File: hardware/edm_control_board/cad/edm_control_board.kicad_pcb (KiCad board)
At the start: 2 copper layers, 240 x 100 mm, 60 parts, among them J501 Conn_02x08_Odd_Even, J502 Conn_01x02, Q201 BSS214NW, Q202 BSS214NW, Q203 BSS214NW, Q204 BSS214NW, SW401 SW_Push, SW402 SW_Push, SW403 SW_Push, SW404 SW_Push, U301 STM32F722RETx, U302 R-78E3.3-1.0, U303 L78L05_SO8, U401 NHD-0420H1Z, Y201 25M

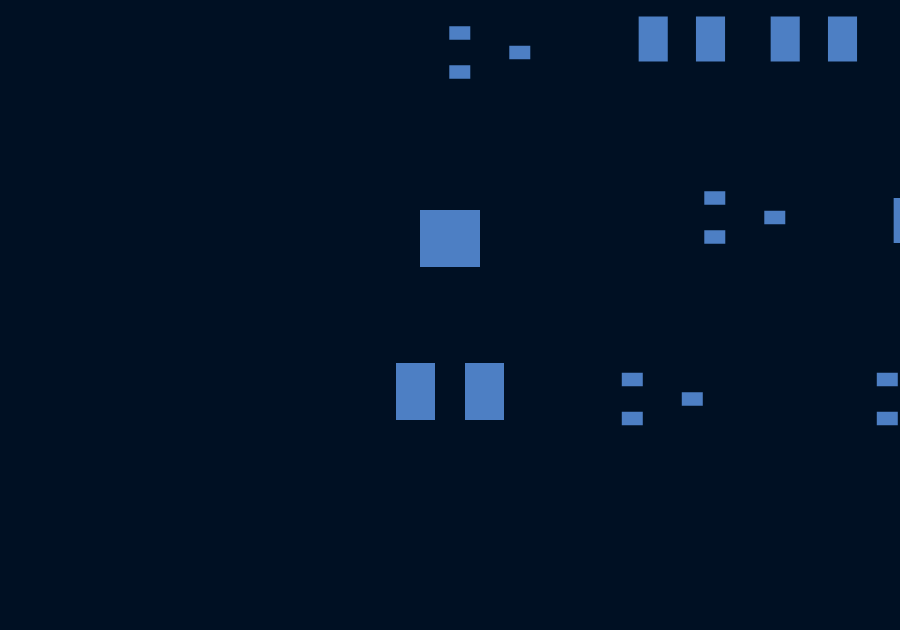
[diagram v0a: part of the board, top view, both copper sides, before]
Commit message: Change to horizontal trim pot
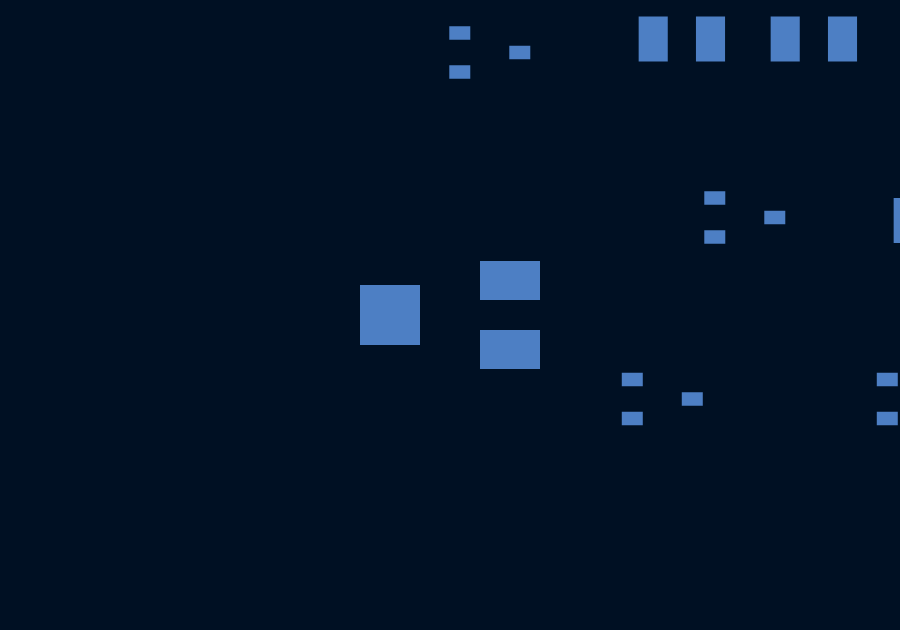
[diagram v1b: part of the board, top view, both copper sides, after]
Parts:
- RV201: footprint Potentiometer_SMD:Potentiometer_Bourns_3214X_Vertical -> Potentiometer_SMD:Potentiometer_Bourns_3214J_Horizontal
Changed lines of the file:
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@@
     (add_net "Net-(U303-Pad5)")
+  )
+  (module Potentiometer_SMD:Potentiometer_Bourns_3214J_Horizontal (layer B.Cu)
+    (at 108.43505 -117.520679)
+    (descr "Potentiometer, horizontal, Bourns 3214J, https://www.bourns.com/docs/Product-Datasheets/3214.pdf")
+    (tags "Potentiometer horizontal Bourns 3214J")
+    (attr smd)
+    (fp_text reference RV201 (at 0 3.65) (layer B.SilkS)
+      (effects (font (size 1 1) (thickness 0.15)) (justify mirror))
+    )
+    (fp_text value 20k (at 0 -3.65) (layer B.Fab)
+      (effects (font (size 1 1) (thickness 0.15)) (justify mirror))
+    )
+    (fp_line (start -2.3 2.4) (end -2.3 -2.4) (layer B.Fab) (width 0.1))
+    (fp_line (start -2.3 -2.4) (end 2.3 -2.4) (layer B.Fab) (width 0.1))
+    (fp_line (start 2.3 -2.4) (end 2.3 2.4) (layer B.Fab) (width 0.1))
+    (fp_line (start 2.3 2.4) (end -2.3 2.4) (layer B.Fab) (width 0.1))
+    (fp_line (start -2.3 2.02) (end -2.3 0.24) (layer B.Fab) (width 0.1))
+    (fp_line (start -2.3 0.24) (end -2.3 0.24) (layer B.Fab) (width 0.1))
+    (fp_line (start -2.3 0.24) (end -2.3 2.02) (layer B.Fab) (width 0.1))
+    (fp_line (start -2.3 2.02) (end -2.3 2.02) (layer B.Fab) (width 0.1))
+    (fp_line (start -2.3 1.13) (end -2.3 1.13) (layer B.Fab) (width 0.1))
+    (fp_line (start -2.42 2.52) (end 2.42 2.52) (layer B.SilkS) (width 0.12))
+    (fp_line (start -2.42 -2.52) (end 2.42 -2.52) (layer B.SilkS) (width 0.12))
+    (fp_line (start -2.42 2.52) (end -2.42 1.24) (layer B.SilkS) (width 0.12))
+    (fp_line (start -2.42 -1.24) (end -2.42 -2.52) (layer B.SilkS) (width 0.12))
+    (fp_line (start 2.42 2.52) (end 2.42 2.04) (layer B.SilkS) (width 0.12))
+    (fp_line (start 2.42 0.26) (end 2.42 -0.26) (layer B.SilkS) (width 0.12))
+    (fp_line (start 2.42 -2.04) (end 2.42 -2.52) (layer B.SilkS) (width 0.12))
+    (fp_line (start -2.42 2.14) (end -2.42 2.14) (layer B.SilkS) (width 0.12))
+    (fp_line (start -2.42 2.14) (end -2.42 1.24) (layer B.SilkS) (width 0.12))
+    (fp_line (start -2.42 2.14) (end -2.42 1.24) (layer B.SilkS) (width 0.12))
+    (fp_line (start -3.25 2.65) (end -3.25 -2.65) (layer B.CrtYd) (width 0.05))
+    (fp_line (start -3.25 -2.65) (end 3.25 -2.65) (layer B.CrtYd) (width 0.05))
+    (fp_line (start 3.25 -2.65) (end 3.25 2.65) (layer B.CrtYd) (width 0.05))
+    (fp_line (start 3.25 2.65) (end -3.25 2.65) (layer B.CrtYd) (width 0.05))
+    (fp_text user %R (at 0 0) (layer B.Fab)
+      (effects (font (size 1 1) (thickness 0.15)) (justify mirror))
+    )
+    (pad 1 smd rect (at 2 1.15) (size 2 1.3) (layers B.Cu B.Paste B.Mask)
+      (net 16 +3V3))
+    (pad 2 smd rect (at -2 0) (size 2 2) (layers B.Cu B.Paste B.Mask)
+      (net 60 /Controller/LCD_V0))
+    (pad 3 smd rect (at 2 -1.15) (size 2 1.3) (layers B.Cu B.Paste B.Mask)
+      (net 14 GND))
+    (model ${KISYS3DMOD}/Potentiometer_SMD.3dshapes/Potentiometer_Bourns_3214J_Horizontal.wrl
+      (at (xyz 0 0 0))
+      (scale (xyz 1 1 1))
+      (rotate (xyz 0 0 0))
+    )
   )
   (module Capacitor_SMD:C_0805_2012Metric (layer B.Cu)
@@
       (at (xyz 0 0 0))
       (scale (xyz 1 1 1))
-      (rotate (xyz 0 0 0))
-    )
-  )
-  (module Potentiometer_SMD:Potentiometer_Bourns_3214X_Vertical (layer B.Cu)
-    (at 108.43505 -117.520679)
-    (descr "Potentiometer, vertical, Bourns 3214X, https://www.bourns.com/docs/Product-Datasheets/3214.pdf")
-    (tags "Potentiometer vertical Bourns 3214X")
-    (attr smd)
-    (fp_text reference RV201 (at -0.1 4.75) (layer B.SilkS)
-      (effects (font (size 1 1) (thickness 0.15)) (justify mirror))
-    )
-    (fp_text value 20k (at -0.1 -4.75) (layer B.Fab)
-      (effects (font (size 1 1) (thickness 0.15)) (justify mirror))
-    )
-    (fp_circle (center -1.3 -0.65) (end -0.55 -0.65) (layer B.Fab) (width 0.1))
-    (fp_line (start -2.5 1.75) (end -2.5 -1.75) (layer B.Fab) (width 0.1))
-    (fp_line (start -2.5 -1.75) (end 2.3 -1.75) (layer B.Fab) (width 0.1))
-    (fp_line (start 2.3 -1.75) (end 2.3 1.75) (layer B.Fab) (width 0.1))
-    (fp_line (start 2.3 1.75) (end -2.5 1.75) (layer B.Fab) (width 0.1))
-    (fp_line (start -1.3 -1.393) (end -1.299 0.092) (layer B.Fab) (width 0.1))
-    (fp_line (start -1.3 -1.393) (end -1.299 0.092) (layer B.Fab) (width 0.1))
-    (fp_line (start 2.04 1.87) (end 2.42 1.87) (layer B.SilkS) (width 0.12))
-    (fp_line (start -2.62 1.87) (end -2.039 1.87) (layer B.SilkS) (width 0.12))
-    (fp_line (start -0.26 1.87) (end 0.26 1.87) (layer B.SilkS) (width 0.12))
-    (fp_line (start -2.62 -1.87) (end -1.24 -1.87) (layer B.SilkS) (width 0.12))
-    (fp_line (start 1.24 -1.87) (end 2.42 -1.87) (layer B.SilkS) (width 0.12))
-    (fp_line (start -2.62 1.87) (end -2.62 -1.87) (layer B.SilkS) (width 0.12))
-    (fp_line (start 2.42 1.87) (end 2.42 -1.87) (layer B.SilkS) (width 0.12))
-    (fp_line (start -2.75 3.75) (end -2.75 -3.75) (layer B.CrtYd) (width 0.05))
-    (fp_line (start -2.75 -3.75) (end 2.55 -3.75) (layer B.CrtYd) (width 0.05))
-    (fp_line (start 2.55 -3.75) (end 2.55 3.75) (layer B.CrtYd) (width 0.05))
-    (fp_line (start 2.55 3.75) (end -2.75 3.75) (layer B.CrtYd) (width 0.05))
-    (fp_text user %R (at 0.5 0) (layer B.Fab)
-      (effects (font (size 0.6 0.6) (thickness 0.15)) (justify mirror))
-    )
-    (pad 1 smd rect (at 1.15 2.55) (size 1.3 1.9) (layers B.Cu B.Paste B.Mask)
-      (net 16 +3V3))
-    (pad 2 smd rect (at 0 -2.55) (size 2 1.9) (layers B.Cu B.Paste B.Mask)
-      (net 60 /Controller/LCD_V0))
-    (pad 3 smd rect (at -1.15 2.55) (size 1.3 1.9) (layers B.Cu B.Paste B.Mask)
-      (net 14 GND))
-    (model ${KISYS3DMOD}/Potentiometer_SMD.3dshapes/Potentiometer_Bourns_3214X_Vertical.wrl
-      (at (xyz 0 0 0))
-      (scale (xyz 1 1 1))

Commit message: Component placement
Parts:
- moved NT301 169.4 mm to (198.0, -8.00)
- moved C208 159.6 mm to (185.5, -60.5)
- moved C209 159.3 mm to (184.5, -52.0)
- moved Y201 159.2 mm to (181.5, -59.4), turned to 270 degrees
- moved R206 158.8 mm to (184.5, -54.5)
- moved C210 150.3 mm to (185.5, -58.0)
- moved R207 149.5 mm to (171.5, -70.0), turned to 90 degrees
- moved C212 146.1 mm to (168.0, -45.5), turned to 180 degrees
- moved C302 142.2 mm to (185.5, -26.5), turned to 90 degrees
- moved C304 137.8 mm to (171.5, -26.5), turned to 90 degrees
- moved C211 137.6 mm to (168.0, -48.0), turned to 180 degrees
- moved U302 131.3 mm to (195.0, -87.0), turned to 90 degrees
- moved C306 127.2 mm to (178.5, -35.0)
- moved U303 123.7 mm to (178.5, -27.5)
- moved C301 118.4 mm to (208.0, -88.0), turned to 90 degrees
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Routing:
- added copper zone on In1.Cu, net +3V3
- added copper zone on In2.Cu, net GND
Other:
- copper layers 2 -> 4

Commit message: Update pinout
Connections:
- U301 pad 14: /Controller/LCD_DB0 -> Net-(U301-Pad14)
- U301 pad 15: /Controller/LCD_DB1 -> Net-(U301-Pad15)
- U301 pad 16: /Controller/LCD_DB2 -> Net-(U301-Pad16)
- U301 pad 17: /Controller/LCD_DB3 -> Net-(U301-Pad17)
- U301 pad 20: /Controller/LCD_DB4 -> /Connectors/Breakdown
- U301 pad 21: /Controller/LCD_DB5 -> /Connectors/Short_Circuit
- U301 pad 22: /Controller/LCD_DB6 -> /Connectors/Output_20V_Enable
- U301 pad 23: /Controller/LCD_DB7 -> /Connectors/Output_250V_Enable
- U301 pad 25: /Connectors/Spark_Voltage_0 -> /Connectors/Spark_Voltage_Status
- U301 pad 26: /Connectors/Spark_Voltage_1 -> /Connectors/Spark_Voltage_2
- U301 pad 27: /Connectors/Spark_Voltage_2 -> /Connectors/Spark_Voltage_1
- U301 pad 28: Net-(U301-Pad28) -> /Connectors/Spark_Voltage_0
- U301 pad 33: Net-(U301-Pad33) -> Net-(Q204-Pad1)
- U301 pad 34: Net-(U301-Pad34) -> Net-(Q203-Pad1)
- U301 pad 35: Net-(U301-Pad35) -> Net-(Q202-Pad1)
- U301 pad 36: Net-(U301-Pad36) -> Net-(Q201-Pad1)
- U301 pad 41: /Controller/LCD_RS -> Net-(U301-Pad41)
- U301 pad 42: /Controller/LCD_RW -> /Controller/LCD_DB1
- U301 pad 43: /Controller/LCD_E -> /Controller/LCD_DB0
- U301 pad 44: Net-(U301-Pad44) -> /Controller/LCD_E
- U301 pad 45: Net-(Q202-Pad1) -> /Controller/LCD_RW
- U301 pad 46: Net-(Q203-Pad1) -> /Controller/LCD_RS
- U301 pad 49: Net-(Q204-Pad1) -> Net-(U301-Pad49)
- U301 pad 50: Net-(Q201-Pad1) -> Net-(U301-Pad50)
- U301 pad 53: Net-(U301-Pad53) -> /Controller/LCD_DB7
- U301 pad 55: /Connectors/Spark_Voltage_Status -> /Controller/LCD_DB6
- U301 pad 56: /Connectors/Output_250V_Enable -> /Controller/LCD_DB5
- U301 pad 57: /Connectors/Output_20V_Enable -> /Controller/LCD_DB4
- U301 pad 58: /Connectors/Short_Circuit -> /Controller/LCD_DB3
- U301 pad 59: /Connectors/Breakdown -> /Controller/LCD_DB2

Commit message: Update pinout
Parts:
- moved C208 1.50 mm to (185.5, -62.0)
- moved C210 1.50 mm to (185.5, -59.5)
- moved Y201 1.50 mm to (181.5, -60.9)
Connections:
- RV401 pad 2: /User Interface/POT_1 -> /Controller/POT_1
- RV402 pad 2: /User Interface/POT_2 -> /Controller/POT_2
- RV403 pad 2: /User Interface/POT_3 -> /Controller/POT_3
- RV404 pad 2: /User Interface/POT_4 -> /Controller/POT_4
- SW401 pad 1: /User Interface/SW_1 -> /Controller/SW_1
- SW402 pad 1: /User Interface/SW_2 -> /Controller/SW_2
- SW403 pad 1: /User Interface/SW_3 -> /Controller/SW_3
- SW404 pad 1: /User Interface/SW_4 -> /Controller/SW_4
- U301 pad 10: Net-(U301-Pad10) -> /Controller/POT_3
- U301 pad 11: Net-(U301-Pad11) -> /Controller/POT_4
- U301 pad 36: Net-(Q201-Pad1) -> Net-(U301-Pad36)
- U301 pad 37: Net-(U301-Pad37) -> /Controller/SW_1
- U301 pad 38: Net-(U301-Pad38) -> /Controller/SW_2
- U301 pad 39: Net-(U301-Pad39) -> /Controller/SW_3
- U301 pad 40: Net-(U301-Pad40) -> /Controller/SW_4
- U301 pad 41: Net-(U301-Pad41) -> /Controller/LCD_DB1
- U301 pad 42: /Controller/LCD_DB1 -> /Controller/LCD_DB0
- U301 pad 43: /Controller/LCD_DB0 -> /Controller/LCD_E
- U301 pad 44: /Controller/LCD_E -> /Controller/LCD_RW
- U301 pad 45: /Controller/LCD_RW -> /Controller/LCD_RS
- U301 pad 46: /Controller/LCD_RS -> Net-(Q201-Pad1)
- U301 pad 49: Net-(U301-Pad49) -> /Controller/LCD_DB7
- U301 pad 50: Net-(U301-Pad50) -> /Controller/LCD_DB6
- U301 pad 51: Net-(U301-Pad51) -> /Controller/LCD_DB5
- U301 pad 52: Net-(U301-Pad52) -> /Controller/LCD_DB4
- U301 pad 53: /Controller/LCD_DB7 -> /Controller/LCD_DB3
- U301 pad 55: /Controller/LCD_DB6 -> /Controller/LCD_DB2
- U301 pad 56: /Controller/LCD_DB5 -> Net-(U301-Pad56)
- U301 pad 57: /Controller/LCD_DB4 -> Net-(U301-Pad57)
- U301 pad 58: /Controller/LCD_DB3 -> Net-(U301-Pad58)
- U301 pad 59: /Controller/LCD_DB2 -> Net-(U301-Pad59)
- U301 pad 8: Net-(U301-Pad8) -> /Controller/POT_1
- U301 pad 9: Net-(U301-Pad9) -> /Controller/POT_2
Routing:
- net /Controller/LCD_RS: track 0.00 -> 105.9 mm
- net /Controller/SW_4: track 0.00 -> 91.4 mm
- net /Controller/POT_4: track 0.00 -> 89.6 mm
- net /Controller/SW_3: track 0.00 -> 87.9 mm
- net /Controller/SW_2: track 0.00 -> 81.3 mm
- net /Controller/LCD_DB7: track 0.00 -> 80.3 mm
- net /Controller/SW_1: track 0.00 -> 79.4 mm
- net /Controller/LCD_DB6: track 0.00 -> 78.1 mm
- net /Controller/LCD_DB2: track 0.00 -> 77.9 mm
- net /Controller/LCD_DB5: track 0.00 -> 77.9 mm
- net /Controller/LCD_DB4: track 0.00 -> 77.9 mm
- net /Controller/LCD_DB3: track 0.00 -> 77.8 mm
- net /Controller/LCD_RW: track 0.00 -> 68.3 mm
- net /Controller/LCD_E: track 0.00 -> 67.8 mm
- net /Controller/LCD_DB0: track 0.00 -> 66.8 mm
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
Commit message: Routing
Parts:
- moved R202 2.18 mm to (159.5, -35.0), turned to 90 degrees
- moved Q202 2.12 mm to (159.5, -31.0), turned to 270 degrees
- moved R203 1.61 mm to (162.5, -35.0), turned to 90 degrees
- moved Q203 1.58 mm to (162.5, -31.0), turned to 270 degrees
- moved Q204 1.58 mm to (165.5, -31.0), turned to 270 degrees
- moved R204 1.58 mm to (165.5, -35.0), turned to 90 degrees
- moved C202 1.20 mm to (179.0, -54.5)
- moved C209 1.12 mm to (183.5, -52.5)
- moved R206 1.12 mm to (183.5, -55.0)
- moved C211 0.81 mm to (167.6, -47.3)
- moved C212 0.81 mm to (167.6, -44.8)
- moved C203 0.50 mm to (175.5, -50.0)
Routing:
- net /Controller/LCD_RW: track 68.3 -> 144.4 mm
- net /Controller/LCD_E: track 67.8 -> 142.4 mm
- net /Controller/LCD_DB0: track 66.8 -> 140.5 mm
- net /Controller/LCD_DB1: track 65.8 -> 138.5 mm
- net GND: track 17.9 -> 86.1 mm, vias 8 -> 25
- net /Controller/POT_3: track 0.00 -> 59.8 mm, vias 0 -> 2
- net /Connectors/Spark_Voltage_0: track 0.00 -> 45.8 mm
- net /Connectors/Spark_Voltage_1: track 0.00 -> 44.0 mm
- net /Connectors/Spark_Voltage_2: track 0.00 -> 42.4 mm
- net /Connectors/Spark_Voltage_Status: track 0.00 -> 40.8 mm
- net /Controller/LCD_RS: track 105.9 -> 146.3 mm
- net /Connectors/Output_250V_Enable: track 0.00 -> 40.2 mm
- net /Controller/POT_1: track 0.00 -> 35.9 mm
- net /Controller/POT_4: track 89.6 -> 58.1 mm, vias 0 -> 2
- net Net-(Q202-Pad1): track 0.00 -> 28.6 mm
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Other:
- net class Pwr added: clearance 0.3, trace_width 0.5, via_dia 0.8, via_drill 0.4

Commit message: Routing
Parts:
- moved NT301 1.60 mm to (199.6, -8.00)
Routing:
- net +24V: track 4.32 -> 151.2 mm
- net /Controller/SW_2: track 81.3 -> 194.7 mm
- net /Controller/SW_4: track 91.4 -> 201.3 mm
- net /Controller/SW_3: track 87.9 -> 153.5 mm
- net /Controller/SW_1: track 79.4 -> 134.3 mm
- net /Connectors/Stepper_EN: track 0.00 -> 35.9 mm
- net +5V: track 4.32 -> 33.3 mm
- net /Connectors/Stepper_DIR: track 0.00 -> 24.1 mm
- net /Connectors/Stepper_PUL: track 0.00 -> 23.3 mm
- net GND: track 86.1 -> 94.5 mm
- net /Controller/POT_4: track 58.1 -> 50.3 mm
- net /Connectors/Breakdown: track 40.5 -> 42.9 mm
- net /Connectors/Spark_Voltage_0: track 45.8 -> 48.0 mm
- net /Connectors/Short_Circuit: track 40.4 -> 41.6 mm
- net /Connectors/Spark_Voltage_1: track 44.0 -> 45.0 mm

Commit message: Add SWD connector
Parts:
- added J405: Conn_01x06, Connector_PinHeader_2.54mm:PinHeader_1x06_P2.54mm_Vertical, B.Cu at (122.1, -91.1)
- added R401: 1M, Resistor_SMD:R_1206_3216Metric, B.Cu at (216.5, -26.3)
- moved C301 13.0 mm to (195.6, -84.2)
- moved C303 13.0 mm to (174.6, -87.2)
- moved C305 13.0 mm to (165.6, -85.2)
- moved U302 13.0 mm to (182.6, -83.2)
- moved J402 1.00 mm to (206.0, -9.00)
- moved NT301 1.00 mm to (199.6, -9.00)
- renumbered J501 to J401, J502 to J402, JJ503 to J403, JJ504 to J404, RV401 to RV501, RV402 to RV502, RV403 to RV503, RV404 to RV504, SW401 to SW501, SW402 to SW502, SW403 to SW503, SW404 to SW504, U401 to U501
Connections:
- J401 pad 1: /Connectors/+3V3 -> +3V3
- J401 pad 11: /Connectors/GND -> GND
- J401 pad 13: /Connectors/GND -> GND
- J401 pad 15: /Connectors/GND -> GND
- J401 pad 3: /Connectors/GND -> GND
- J401 pad 5: /Connectors/GND -> GND
- J401 pad 7: /Connectors/GND -> GND
- J401 pad 9: /Connectors/GND -> GND
- MK501 pad 1: GND -> /Connectors/Shield
- MK502 pad 1: GND -> /Connectors/Shield
- MK503 pad 1: GND -> /Connectors/Shield
- MK504 pad 1: GND -> /Connectors/Shield
- MK505 pad 1: GND -> /Connectors/Shield
- MK506 pad 1: GND -> /Connectors/Shield
- MK507 pad 1: GND -> /Connectors/Shield
- MK508 pad 1: GND -> /Connectors/Shield
- MK509 pad 1: GND -> /Connectors/Shield
- MK510 pad 1: GND -> /Connectors/Shield
- MK511 pad 1: GND -> /Connectors/Shield
- MK512 pad 1: GND -> /Connectors/Shield
- U301 pad 36: Net-(U301-Pad36) -> /Controller/SW_1
- U301 pad 37: /Controller/SW_1 -> /Controller/SW_2
- U301 pad 38: /Controller/SW_2 -> /Controller/SW_3
- U301 pad 39: /Controller/SW_3 -> /Controller/SW_4
- U301 pad 40: /Controller/SW_4 -> /Controller/LCD_DB1
- U301 pad 41: /Controller/LCD_DB1 -> /Controller/LCD_DB0
- U301 pad 42: /Controller/LCD_DB0 -> /Controller/LCD_E
- U301 pad 43: /Controller/LCD_E -> /Controller/LCD_RW
- U301 pad 44: /Controller/LCD_RW -> /Controller/LCD_RS
- U301 pad 45: /Controller/LCD_RS -> Net-(Q201-Pad1)
- U301 pad 46: Net-(Q201-Pad1) -> /Connectors/SWDIO
- U301 pad 49: /Controller/LCD_DB7 -> /Connectors/SWCLK
- U301 pad 50: /Controller/LCD_DB6 -> /Controller/LCD_DB7
- U301 pad 51: /Controller/LCD_DB5 -> /Controller/LCD_DB6
- U301 pad 52: /Controller/LCD_DB4 -> /Controller/LCD_DB5
- U301 pad 53: /Controller/LCD_DB3 -> /Controller/LCD_DB4
- U301 pad 55: /Controller/LCD_DB2 -> /Connectors/SWO
- U301 pad 56: Net-(U301-Pad56) -> /Controller/LCD_DB3
- U301 pad 57: Net-(U301-Pad57) -> /Controller/LCD_DB2
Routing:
- net /Connectors/SWCLK: track 0.00 -> 70.5 mm, vias 0 -> 1
- net /Connectors/SWDIO: track 0.00 -> 61.3 mm, vias 0 -> 1
- net /Connectors/SWO: track 0.00 -> 60.8 mm, vias 0 -> 1
- net /Connectors/Shield: track 0.00 -> 16.4 mm
- net +24V: track 151.2 -> 139.2 mm
- net GND: track 94.5 -> 97.9 mm, vias 25 -> 27
- net /Controller/LCD_DB4: track 77.9 -> 75.2 mm
- net /Controller/LCD_DB5: track 77.9 -> 75.3 mm
- net /Controller/LCD_DB6: track 78.1 -> 75.6 mm
- net /Controller/LCD_DB7: track 80.3 -> 77.8 mm
- net /Controller/LCD_DB2: track 77.9 -> 75.5 mm
- net /Controller/LCD_DB3: track 77.8 -> 75.5 mm
- net /Controller/POT_1: track 35.9 -> 35.0 mm
- net /Controller/SW_3: track 153.5 -> 153.0 mm
- added copper zone on F.Cu, net /Connectors/Shield
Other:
- board text added: "+24V"
- board text added: "+3V3"
- board text added: "1"
- board text added: "BLA"
- board text added: "BLK"
- board text added: "Contrast"
- board text added: "DB0"
- board text added: "DB1"
- board text added: "DB2"
- board text added: "DB3"
- board text added: "DB4"
- board text added: "DB5"
- board text added: "DB6"
- board text added: "DB7"
- board text added: "DIR"
- board text added: "E"
- board text added: "EN"
- board text added: "GND"
- board text added: "NRST"
- board text added: "PUL"
- board text added: "RS"
- board text added: "RW"
- board text added: "SWCLK"
- board text added: "SWDIO"
- board text added: "SWO"
- board text added: "V0"
